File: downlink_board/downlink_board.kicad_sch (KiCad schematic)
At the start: 52 parts, among them J2 SCREEN, J2 USB_C_Receptacle_USB2.0, J3 GPIO, J4 PROGRAM, SW1 MCU_{RST}, SW1 RPi_{ON}, SW2 RPi_{OFF}, U1 nRF24L01, U2 STM32F103C8Tx, U2 TPS563208DDCR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

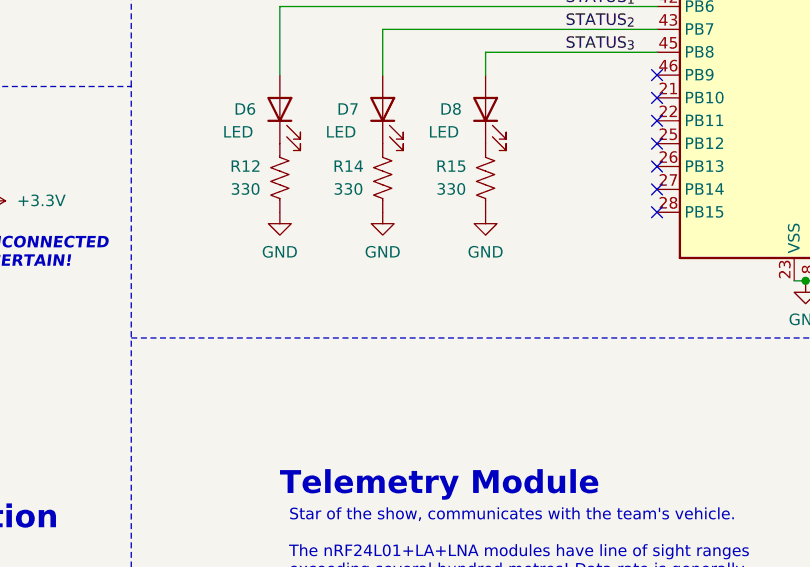
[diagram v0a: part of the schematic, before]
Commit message: Added PWM message for LEDs
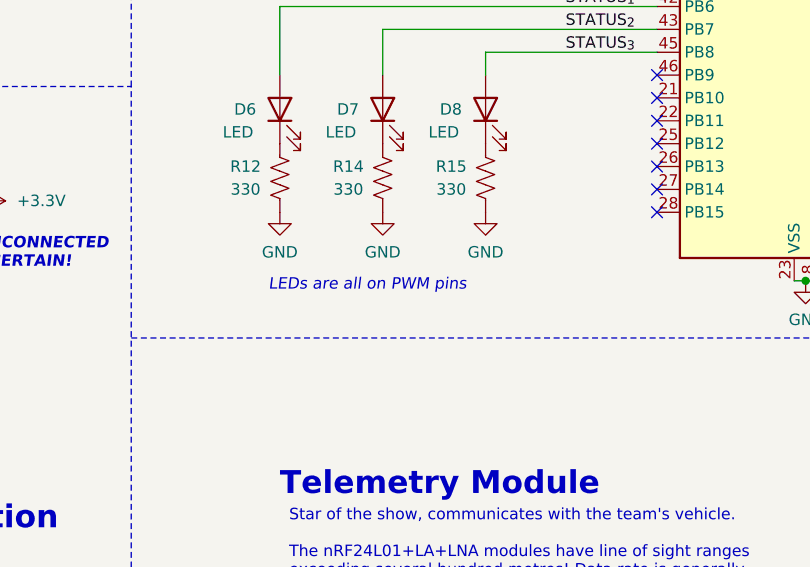
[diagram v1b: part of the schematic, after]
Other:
- note added: "LEDs are all on PWM pins"
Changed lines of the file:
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@@
     (effects (font (size 1.27 1.27)) (justify left bottom))
+  )
+  (text "LEDs are all on PWM pins" (at 133.35 114.3 0)
+    (effects (font (size 1.27 1.27) italic) (justify left bottom))
   )
   (text "Telemetry Module" (at 134.62 137.16 0)

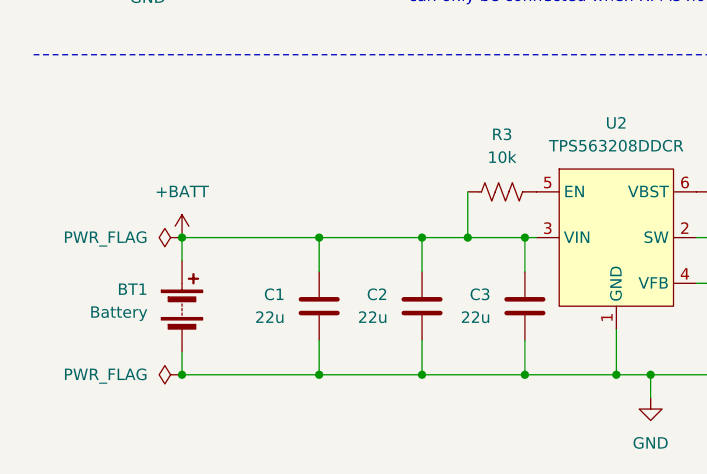
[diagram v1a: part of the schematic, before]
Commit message: Revised input caps for vreg
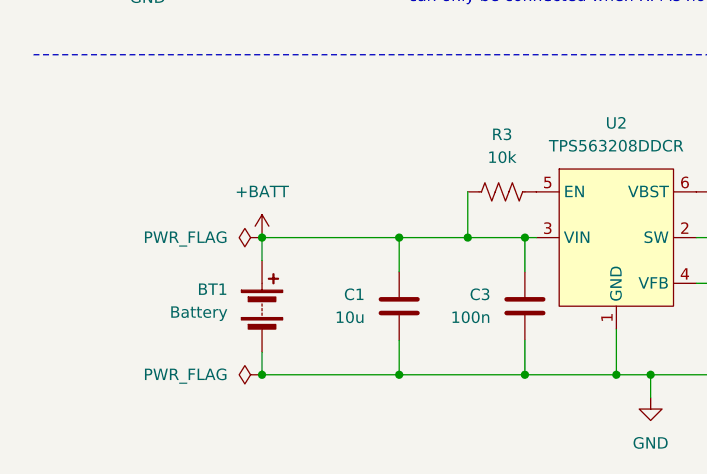
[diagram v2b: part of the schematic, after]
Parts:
- removed C2: 22u, Capacitor_SMD:C_0805_2012Metric, symbol Device:C
- BT1: now left out of the parts list
- C1: footprint Capacitor_SMD:C_0603_1608Metric -> Capacitor_SMD:C_0805_2012Metric
- C1: value 22u -> 10u
- C3: value 22u -> 100n; footprint Capacitor_SMD:C_0805_2012Metric -> Capacitor_SMD:C_0603_1608Metric
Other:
- moved on the sheet: BT1, C1, C3

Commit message: Completed Rev 1.0 layout
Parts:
- C1: footprint Capacitor_SMD:C_0805_2012Metric -> Capacitor_SMD:C_0603_1608Metric
- J4: footprint Connector_PinSocket_2.54mm:PinSocket_1x03_P2.54mm_Vertical -> Connector_PinHeader_2.54mm:PinHeader_1x03_P2.54mm_Vertical
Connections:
- net BATT_{DIV}: now also U2.19 (PB1); no longer U2.10 (PA0)
- net RF_{EN}: now also U2.12 (PA2); no longer U2.19 (PB1)
- net RF_{INT}: now also U2.18 (PB0); no longer U2.14 (PA4)
- net RF_{SEL}: now also U2.13 (PA3); no longer U2.18 (PB0)
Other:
- moved on the sheet: C4, R18, R21
